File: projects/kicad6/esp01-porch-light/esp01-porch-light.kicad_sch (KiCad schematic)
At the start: 15 parts, among them J1 RELAY, J2 Conn_01x02_Male, Q1 2N3904, U1 AMS1117-3.3, U2 ESP01

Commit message: Add porch light updated schematic
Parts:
- removed J1: RELAY, Connector_PinSocket_2.54mm:PinSocket_1x02_P2.54mm_Vertical, symbol Connector:Conn_01x02_Male
- added J1: Relay, Connector_PinSocket_2.54mm:PinSocket_1x03_P2.54mm_Vertical, symbol Connector:Conn_01x03_Female
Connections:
- net +5V: now also J1.1 (Pin_1)
- net GND: now also J1.2 (Pin_2)
- net RELAY_IN: now also J1.3 (Pin_3)
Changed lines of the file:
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@@
     (company "Amitesh Singh")
   )
-  (junction (at 237.49 69.85) (diameter 0) (color 0 0 0 0)
-  )
   (junction (at 157.48 59.69) (diameter 0) (color 0 0 0 0)
   )
@@
   (junction (at 73.66 67.31) (diameter 0) (color 0 0 0 0)
   )
-  (junction (at 237.49 72.39) (diameter 0) (color 0 0 0 0)
-  )
   (junction (at 64.77 76.2) (diameter 0) (color 0 0 0 0)
   )
@@
   (junction (at 153.67 80.01) (diameter 0) (color 0 0 0 0)
   )
-  (junction (at 227.33 72.39) (diameter 0) (color 0 0 0 0)
-  )
   (junction (at 227.33 68.58) (diameter 0) (color 0 0 0 0)
+  )
+  (junction (at 227.33 58.42) (diameter 0) (color 0 0 0 0)
   )
   (junction (at 227.33 69.85) (diameter 0) (color 0 0 0 0)
@@
   (no_connect (at 113.03 67.31))
   (no_connect (at 113.03 74.93))
-  (no_connect (at 113.03 77.47))
+  (no_connect (at 106.68 77.47))
   (wire (pts (xy 73.66 67.31) (xy 73.66 68.58))
     (stroke (width 0) (type default) (color 0 0 0 0))
@@
     (stroke (width 0) (type default) (color 0 0 0 0))
   )
-  (wire (pts (xy 233.68 69.85) (xy 237.49 69.85))
+  (wire (pts (xy 233.68 69.85) (xy 241.3 69.85))
     (stroke (width 0) (type default) (color 0 0 0 0))
   )
@@
     (stroke (width 0) (type default) (color 0 0 0 0))
   )
-  (wire (pts (xy 227.33 72.39) (xy 227.33 73.66))
+  (wire (pts (xy 236.22 58.42) (xy 236.22 64.77))
+    (stroke (width 0) (type default) (color 0 0 0 0))
+  )
+  (wire (pts (xy 227.33 69.85) (xy 227.33 73.66))
     (stroke (width 0) (type default) (color 0 0 0 0))
   )
@@
     (stroke (width 0) (type default) (color 0 0 0 0))
   )
-  (wire (pts (xy 237.49 69.85) (xy 241.3 69.85))
-    (stroke (width 0) (type default) (color 0 0 0 0))
-  )
   (wire (pts (xy 167.64 74.93) (xy 167.64 80.01))
     (stroke (width 0) (type default) (color 0 0 0 0))
@@
     (stroke (width 0) (type default) (color 0 0 0 0))
   )
+  (wire (pts (xy 236.22 67.31) (xy 241.3 67.31))
+    (stroke (width 0) (type default) (color 0 0 0 0))
+  )
   (wire (pts (xy 151.13 59.69) (xy 151.13 64.77))
     (stroke (width 0) (type default) (color 0 0 0 0))
@@
     (stroke (width 0) (type default) (color 0 0 0 0))
   )
+  (wire (pts (xy 227.33 58.42) (xy 227.33 59.69))
+    (stroke (width 0) (type default) (color 0 0 0 0))
+  )
   (wire (pts (xy 203.2 78.74) (xy 208.28 78.74))
     (stroke (width 0) (type default) (color 0 0 0 0))
@@
     (stroke (width 0) (type default) (color 0 0 0 0))
   )
-  (wire (pts (xy 233.68 64.77) (xy 233.68 69.85))
+  (wire (pts (xy 233.68 73.66) (xy 233.68 69.85))
+    (stroke (width 0) (type default) (color 0 0 0 0))
+  )
+  (wire (pts (xy 106.68 77.47) (xy 113.03 77.47))
     (stroke (width 0) (type default) (color 0 0 0 0))
   )
@@
     (stroke (width 0) (type default) (color 0 0 0 0))
   )
-  (wire (pts (xy 237.49 72.39) (xy 241.3 72.39))
-    (stroke (width 0) (type default) (color 0 0 0 0))
-  )
   (wire (pts (xy 227.33 67.31) (xy 227.33 68.58))
     (stroke (width 0) (type default) (color 0 0 0 0))
@@
     (stroke (width 0) (type default) (color 0 0 0 0))
   )
-  (wire (pts (xy 227.33 69.85) (xy 227.33 72.39))
-    (stroke (width 0) (type default) (color 0 0 0 0))
-  )
   (polyline (pts (xy 186.69 49.53) (xy 266.7 49.53))
     (stroke (width 0) (type default) (color 0 0 0 0))
   )
-  (wire (pts (xy 237.49 69.85) (xy 237.49 72.39))
-    (stroke (width 0) (type default) (color 0 0 0 0))
-  )
   (wire (pts (xy 217.17 90.17) (xy 227.33 90.17))
     (stroke (width 0) (type default) (color 0 0 0 0))
@@
     (stroke (width 0) (type default) (color 0 0 0 0))
   )
+  (wire (pts (xy 236.22 64.77) (xy 241.3 64.77))
+    (stroke (width 0) (type default) (color 0 0 0 0))
+  )
   (wire (pts (xy 217.17 78.74) (xy 219.71 78.74))
     (stroke (width 0) (type default) (color 0 0 0 0))
@@
     (stroke (width 0) (type default) (color 0 0 0 0))
   )
-  (wire (pts (xy 227.33 72.39) (xy 237.49 72.39))
-    (stroke (width 0) (type default) (color 0 0 0 0))
-  )
-  (wire (pts (xy 227.33 55.88) (xy 227.33 59.69))
+  (wire (pts (xy 227.33 58.42) (xy 236.22 58.42))
+    (stroke (width 0) (type default) (color 0 0 0 0))
+  )
+  (wire (pts (xy 227.33 55.88) (xy 227.33 58.42))
     (stroke (width 0) (type default) (color 0 0 0 0))
   )
@@
     )
   )
-  (global_label "RELAY_IN" (shape input) (at 233.68 64.77 90) (fields_autoplaced)
+  (global_label "RELAY_IN" (shape input) (at 233.68 73.66 0) (fields_autoplaced)
     (effects (font (size 1.27 1.27)) (justify left))
-    (property "Intersheet References" "${INTERSHEET_REFS}" (id 0) (at 233.6006 53.8298 90)
+    (property "Intersheet References" "${INTERSHEET_REFS}" (id 0) (at 244.6202 73.5806 0)
       (effects (font (size 1.27 1.27)) (justify left) hide)
     )
@@
     (pin "2")
   )
+  (symbol (lib_id "Connector:Conn_01x03_Female") (at 246.38 67.31 0) (unit 1)
+    (in_bom yes) (on_board yes) (fields_autoplaced)
+    (property "Reference" "J1" (id 0) (at 247.65 66.0399 0)
+      (effects (font (size 1.27 1.27)) (justify left))
+    )
+    (property "Value" "Relay" (id 1) (at 247.65 68.5799 0)
+      (effects (font (size 1.27 1.27)) (justify left))
+    )
+    (property "Footprint" "Connector_PinSocket_2.54mm:PinSocket_1x03_P2.54mm_Vertical" (id 2) (at 246.38 67.31 0)
+      (effects (font (size 1.27 1.27)) hide)
+    )
+    (property "Datasheet" "~" (id 3) (at 246.38 67.31 0)
+      (effects (font (size 1.27 1.27)) hide)
+    )
+    (pin "1")
+    (pin "2")
+    (pin "3")
+  )
   (symbol (lib_id "Device:C") (at 160.02 86.36 270) (unit 1)
     (in_bom yes) (on_board yes)
@@
     (pin "1")
   )
-  (symbol (lib_id "Connector:Conn_01x02_Male") (at 246.38 72.39 180) (unit 1)
-    (in_bom yes) (on_board yes) (fields_autoplaced)
-    (property "Reference" "J1" (id 0) (at 247.65 69.8499 0)
-      (effects (font (size 1.27 1.27)) (justify right))
-    )
-    (property "Value" "RELAY" (id 1) (at 247.65 72.3899 0)
-      (effects (font (size 1.27 1.27)) (justify right))
-    )
-    (property "Footprint" "Connector_PinSocket_2.54mm:PinSocket_1x02_P2.54mm_Vertical" (id 2) (at 246.38 72.39 0)
-      (effects (font (size 1.27 1.27)) hide)
-    )
-    (property "Datasheet" "~" (id 3) (at 246.38 72.39 0)
-      (effects (font (size 1.27 1.27)) hide)
-    )
-    (pin "1")
-    (pin "2")
-  )
   (symbol (lib_id "Device:R") (at 227.33 63.5 180) (unit 1)
     (in_bom yes) (on_board yes)
@@
     (pin "1")
     (pin "2")
+  )
+  (symbol (lib_id "power:GND") (at 236.22 67.31 0) (unit 1)
+    (in_bom yes) (on_board yes) (fields_autoplaced)
+    (property "Reference" "#PWR0101" (id 0) (at 236.22 73.66 0)
+      (effects (font (size 1.27 1.27)) hide)
+    )
+    (property "Value" "GND" (id 1) (at 236.22 72.39 0))
+    (property "Footprint" "" (id 2) (at 236.22 67.31 0)
+      (effects (font (size 1.27 1.27)) hide)
+    )
+    (property "Datasheet" "" (id 3) (at 236.22 67.31 0)
+      (effects (font (size 1.27 1.27)) hide)
+    )
+    (pin "1")
   )
   (symbol (lib_id "power:GND") (at 151.13 82.55 0) (unit 1)
@@
       (reference "#PWR09") (unit 1) (value "+5V") (footprint "")
     )
+    (path "/866e34f3-1514-4de0-8aef-6758eb670759"
+      (reference "#PWR0101") (unit 1) (value "GND") (footprint "")
+    )
     (path "/38da70ef-24e2-4907-8cff-cb43c20d7fb2"
       (reference "C1") (unit 1) (value "10u") (footprint "Capacitor_SMD:C_0805_2012Metric_Pad1.18x1.45mm_HandSolder")
@@
       (reference "C5") (unit 1) (value "0.1u") (footprint "Capacitor_SMD:C_0805_2012Metric_Pad1.18x1.45mm_HandSolder")
     )
-    (path "/63bc6a2d-254a-4a3b-a312-5926d1249412"
-      (reference "J1") (unit 1) (value "RELAY") (footprint "Connector_PinSocket_2.54mm:PinSocket_1x02_P2.54mm_Vertical")
+    (path "/11df0a9a-26d0-409f-990a-49d7323fbb2a"
+      (reference "J1") (unit 1) (value "Relay") (footprint "Connector_PinSocket_2.54mm:PinSocket_1x03_P2.54mm_Vertical")
     )
     (path "/bf979571-9cfa-40e2-8f58-0a6dd22b17e2"

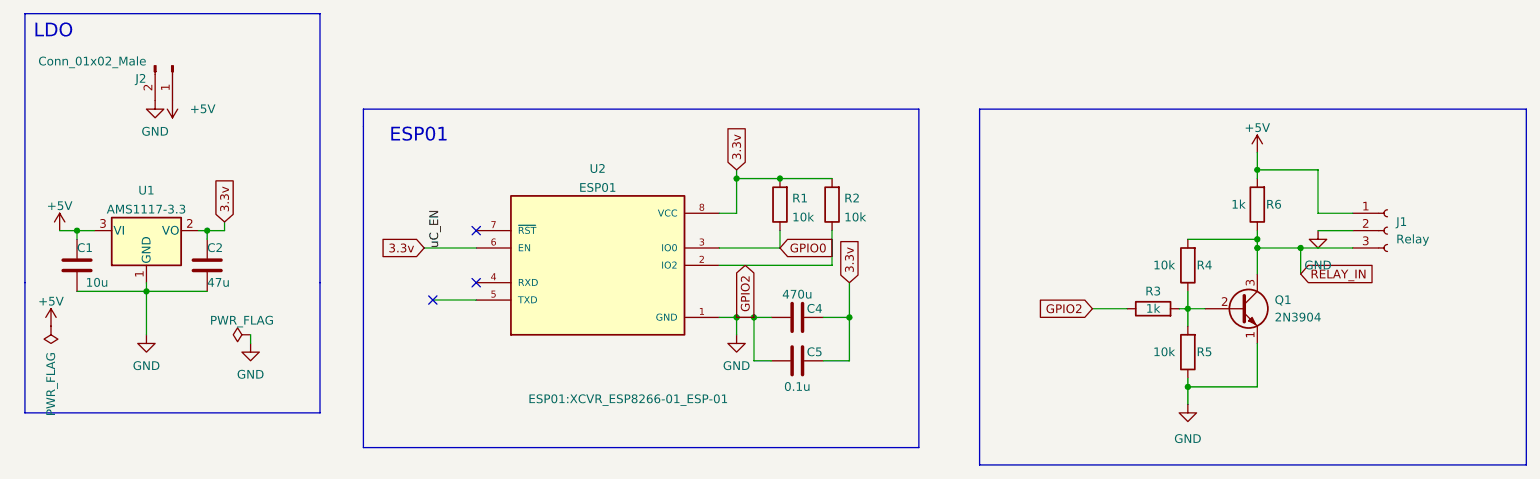
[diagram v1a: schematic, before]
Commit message: update esp 01 port light PCB
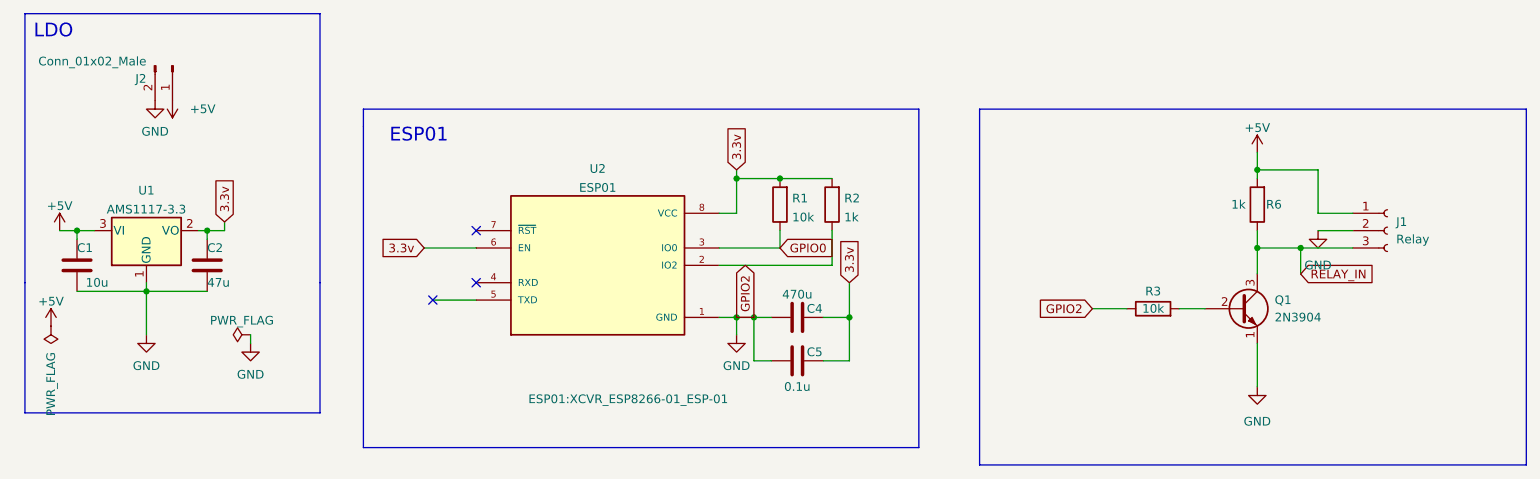
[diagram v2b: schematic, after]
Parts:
- removed R4, R5: 10k, Resistor_SMD:R_0805_2012Metric_Pad1.20x1.40mm_HandSolder, symbol Device:R
- C4: footprint Capacitor_THT:C_Radial_D4.0mm_H7.0mm_P1.50mm -> Capacitor_THT:C_Radial_D10.0mm_H20.0mm_P5.00mm
- R2: value 10k -> 1k
- R3: value 1k -> 10k
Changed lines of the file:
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@@
   (junction (at 157.48 59.69) (diameter 0) (color 0 0 0 0)
   )
-  (junction (at 217.17 78.74) (diameter 0) (color 0 0 0 0)
-  )
   (junction (at 151.13 80.01) (diameter 0) (color 0 0 0 0)
   )
   (junction (at 233.68 69.85) (diameter 0) (color 0 0 0 0)
   )
-  (junction (at 217.17 90.17) (diameter 0) (color 0 0 0 0)
-  )
   (junction (at 73.66 67.31) (diameter 0) (color 0 0 0 0)
   )
@@
   )
   (junction (at 153.67 80.01) (diameter 0) (color 0 0 0 0)
-  )
-  (junction (at 227.33 68.58) (diameter 0) (color 0 0 0 0)
   )
   (junction (at 227.33 58.42) (diameter 0) (color 0 0 0 0)
@@
     (stroke (width 0) (type default) (color 0 0 0 0))
   )
-  (wire (pts (xy 227.33 68.58) (xy 227.33 69.85))
-    (stroke (width 0) (type default) (color 0 0 0 0))
-  )
   (wire (pts (xy 227.33 83.82) (xy 227.33 90.17))
     (stroke (width 0) (type default) (color 0 0 0 0))
@@
     (stroke (width 0) (type default) (color 0 0 0 0))
   )
-  (wire (pts (xy 217.17 81.28) (xy 217.17 78.74))
-    (stroke (width 0) (type default) (color 0 0 0 0))
-  )
-  (wire (pts (xy 217.17 76.2) (xy 217.17 78.74))
-    (stroke (width 0) (type default) (color 0 0 0 0))
-  )
   (wire (pts (xy 157.48 69.85) (xy 157.48 67.31))
     (stroke (width 0) (type default) (color 0 0 0 0))
@@
     (stroke (width 0) (type default) (color 0 0 0 0))
   )
-  (wire (pts (xy 217.17 90.17) (xy 217.17 88.9))
-    (stroke (width 0) (type default) (color 0 0 0 0))
-  )
   (wire (pts (xy 64.77 74.93) (xy 64.77 76.2))
     (stroke (width 0) (type default) (color 0 0 0 0))
@@
     (stroke (width 0) (type default) (color 0 0 0 0))
   )
-  (wire (pts (xy 217.17 92.71) (xy 217.17 90.17))
-    (stroke (width 0) (type default) (color 0 0 0 0))
-  )
   (wire (pts (xy 163.83 86.36) (xy 167.64 86.36))
     (stroke (width 0) (type default) (color 0 0 0 0))
@@
     (stroke (width 0) (type default) (color 0 0 0 0))
   )
-  (wire (pts (xy 217.17 68.58) (xy 227.33 68.58))
-    (stroke (width 0) (type default) (color 0 0 0 0))
-  )
   (wire (pts (xy 151.13 59.69) (xy 157.48 59.69))
     (stroke (width 0) (type default) (color 0 0 0 0))
@@
     (stroke (width 0) (type default) (color 0 0 0 0))
   )
-  (wire (pts (xy 227.33 67.31) (xy 227.33 68.58))
+  (wire (pts (xy 227.33 67.31) (xy 227.33 69.85))
     (stroke (width 0) (type default) (color 0 0 0 0))
   )
@@
     (stroke (width 0) (type default) (color 0 0 0 0))
   )
-  (wire (pts (xy 217.17 90.17) (xy 227.33 90.17))
-    (stroke (width 0) (type default) (color 0 0 0 0))
-  )
   (wire (pts (xy 54.61 67.31) (xy 57.15 67.31))
     (stroke (width 0) (type default) (color 0 0 0 0))
@@
     (stroke (width 0) (type default) (color 0 0 0 0))
   )
-  (wire (pts (xy 217.17 78.74) (xy 219.71 78.74))
+  (wire (pts (xy 215.9 78.74) (xy 219.71 78.74))
     (stroke (width 0) (type default) (color 0 0 0 0))
   )
@@
   )
   (polyline (pts (xy 46.99 74.93) (xy 46.99 93.98))
-    (stroke (width 0) (type default) (color 0 0 0 0))
-  )
-  (wire (pts (xy 215.9 78.74) (xy 217.17 78.74))
     (stroke (width 0) (type default) (color 0 0 0 0))
   )
@@
   (text "LDO" (at 48.26 39.37 0)
     (effects (font (size 2 2)) (justify left bottom))
-  )
-  (label "uC_EN" (at 107.95 69.85 90)
-    (effects (font (size 1.27 1.27)) (justify left bottom))
   )
   (global_label "GPIO2" (shape input) (at 203.2 78.74 180) (fields_autoplaced)
@@
     (property "Reference" "C4" (id 0) (at 162.56 78.74 90))
     (property "Value" "470u" (id 1) (at 160.02 76.6596 90))
-    (property "Footprint" "Capacitor_THT:C_Radial_D4.0mm_H7.0mm_P1.50mm" (id 2) (at 156.21 80.9752 0)
+    (property "Footprint" "Capacitor_THT:C_Radial_D10.0mm_H20.0mm_P5.00mm" (id 2) (at 156.21 80.9752 0)
       (effects (font (size 1.27 1.27)) hide)
     )
@@
     (pin "1")
   )
-  (symbol (lib_id "power:GND") (at 217.17 92.71 0) (unit 1)
-    (in_bom yes) (on_board yes) (fields_autoplaced)
-    (property "Reference" "#PWR07" (id 0) (at 217.17 99.06 0)
-      (effects (font (size 1.27 1.27)) hide)
-    )
-    (property "Value" "GND" (id 1) (at 217.17 97.79 0))
-    (property "Footprint" "" (id 2) (at 217.17 92.71 0)
-      (effects (font (size 1.27 1.27)) hide)
-    )
-    (property "Datasheet" "" (id 3) (at 217.17 92.71 0)
+  (symbol (lib_id "power:GND") (at 227.33 90.17 0) (unit 1)
+    (in_bom yes) (on_board yes) (fields_autoplaced)
+    (property "Reference" "#PWR07" (id 0) (at 227.33 96.52 0)
+      (effects (font (size 1.27 1.27)) hide)
+    )
+    (property "Value" "GND" (id 1) (at 227.33 95.25 0))
+    (property "Footprint" "" (id 2) (at 227.33 90.17 0)
+      (effects (font (size 1.27 1.27)) hide)
+    )
+    (property "Datasheet" "" (id 3) (at 227.33 90.17 0)
       (effects (font (size 1.27 1.27)) hide)
     )
@@
     (pin "2")
   )
-  (symbol (lib_id "Device:R") (at 217.17 85.09 180) (unit 1)
-    (in_bom yes) (on_board yes)
-    (property "Reference" "R5" (id 0) (at 218.44 85.09 0)
-      (effects (font (size 1.27 1.27)) (justify right))
-    )
-    (property "Value" "10k" (id 1) (at 212.09 85.09 0)
-      (effects (font (size 1.27 1.27)) (justify right))
-    )
-    (property "Footprint" "Resistor_SMD:R_0805_2012Metric_Pad1.20x1.40mm_HandSolder" (id 2) (at 218.948 85.09 90)
-      (effects (font (size 1.27 1.27)) hide)
-    )
-    (property "Datasheet" "~" (id 3) (at 217.17 85.09 0)
-      (effects (font (size 1.27 1.27)) hide)
-    )
-    (pin "1")
-    (pin "2")
-  )
   (symbol (lib_id "power:GND") (at 236.22 67.31 0) (unit 1)
     (in_bom yes) (on_board yes) (fields_autoplaced)
@@
     (in_bom yes) (on_board yes)
     (property "Reference" "R3" (id 0) (at 212.09 76.2 90))
-    (property "Value" "1k" (id 1) (at 212.09 78.74 90))
+    (property "Value" "10k" (id 1) (at 212.09 78.74 90))
     (property "Footprint" "Resistor_SMD:R_0805_2012Metric_Pad1.20x1.40mm_HandSolder" (id 2) (at 212.09 80.518 90)
       (effects (font (size 1.27 1.27)) hide)
@@
     (pin "2")
   )
-  (symbol (lib_id "Device:R") (at 217.17 72.39 180) (unit 1)
-    (in_bom yes) (on_board yes)
-    (property "Reference" "R4" (id 0) (at 218.44 72.39 0)
-      (effects (font (size 1.27 1.27)) (justify right))
-    )
-    (property "Value" "10k" (id 1) (at 212.09 72.39 0)
-      (effects (font (size 1.27 1.27)) (justify right))
-    )
-    (property "Footprint" "Resistor_SMD:R_0805_2012Metric_Pad1.20x1.40mm_HandSolder" (id 2) (at 218.948 72.39 90)
-      (effects (font (size 1.27 1.27)) hide)
-    )
-    (property "Datasheet" "~" (id 3) (at 217.17 72.39 0)
-      (effects (font (size 1.27 1.27)) hide)
-    )
-    (pin "1")
-    (pin "2")
-  )
   (symbol (lib_id "power:+5V") (at 52.07 67.31 0) (unit 1)
     (in_bom yes) (on_board yes) (fields_autoplaced)
@@
       (effects (font (size 1.27 1.27)) (justify right))
     )
-    (property "Value" "10k" (id 1) (at 166.878 65.3666 0)
+    (property "Value" "1k" (id 1) (at 166.878 65.3666 0)
       (effects (font (size 1.27 1.27)) (justify right))
     )
@@
     )
     (path "/1178be57-3e44-4c08-8223-8fb2974077ee"
-      (reference "C4") (unit 1) (value "470u") (footprint "Capacitor_THT:C_Radial_D4.0mm_H7.0mm_P1.50mm")
+      (reference "C4") (unit 1) (value "470u") (footprint "Capacitor_THT:C_Radial_D10.0mm_H20.0mm_P5.00mm")
     )
     (path "/20cb6c7c-21a2-4704-9fae-202efebc737d"
@@
     )
     (path "/e47107be-a2a5-4632-9fa0-a8626a1bfbf7"
-      (reference "R2") (unit 1) (value "10k") (footprint "Resistor_SMD:R_0805_2012Metric_Pad1.20x1.40mm_HandSolder")
+      (reference "R2") (unit 1) (value "1k") (footprint "Resistor_SMD:R_0805_2012Metric_Pad1.20x1.40mm_HandSolder")
     )
     (path "/a5f2c6a6-39af-4d56-9c9b-76b3b222b1a9"
-      (reference "R3") (unit 1) (value "1k") (footprint "Resistor_SMD:R_0805_2012Metric_Pad1.20x1.40mm_HandSolder")
-    )
-    (path "/c8d6303f-e7d0-4e61-a5ec-5a769ec75ae2"
-      (reference "R4") (unit 1) (value "10k") (footprint "Resistor_SMD:R_0805_2012Metric_Pad1.20x1.40mm_HandSolder")
-    )
-    (path "/8179c67d-685e-449a-baec-1b5bfaecff71"
-      (reference "R5") (unit 1) (value "10k") (footprint "Resistor_SMD:R_0805_2012Metric_Pad1.20x1.40mm_HandSolder")
+      (reference "R3") (unit 1) (value "10k") (footprint "Resistor_SMD:R_0805_2012Metric_Pad1.20x1.40mm_HandSolder")
     )
     (path "/76a36846-4b97-40e6-bb07-d0f404348898"
